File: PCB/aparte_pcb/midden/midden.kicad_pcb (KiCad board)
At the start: 2 copper layers, 211 x 207.2 mm, 39 parts, among them J1 Conn_01x10_Socket, J4 Conn_01x10_Socket, J5 Conn_01x04_Socket, K1 G5Q-1A, SW1 SW_Reed_SPDT, SW2 SW_DIP_x01

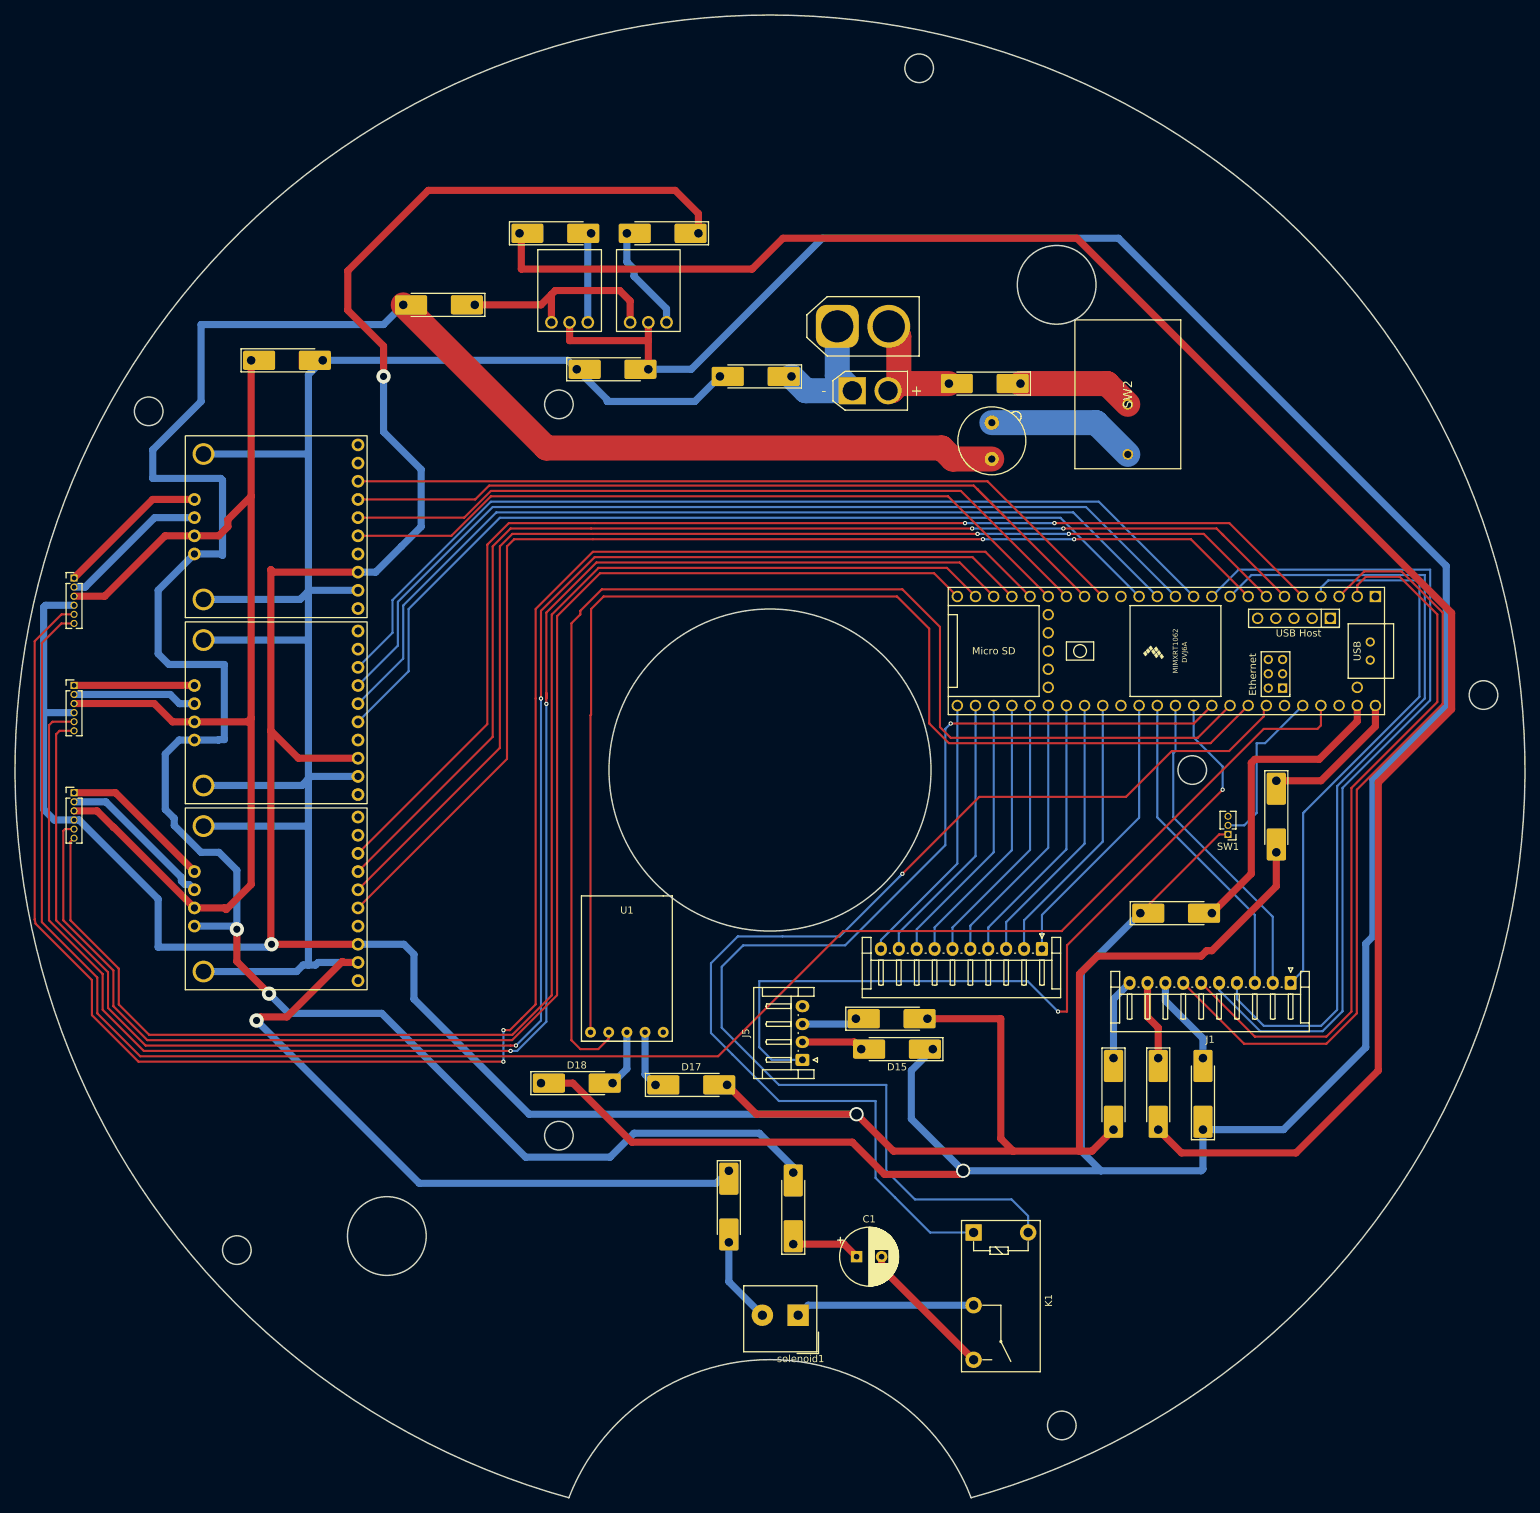
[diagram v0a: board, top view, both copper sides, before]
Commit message: schroef geaard
moet nog onderste schroef
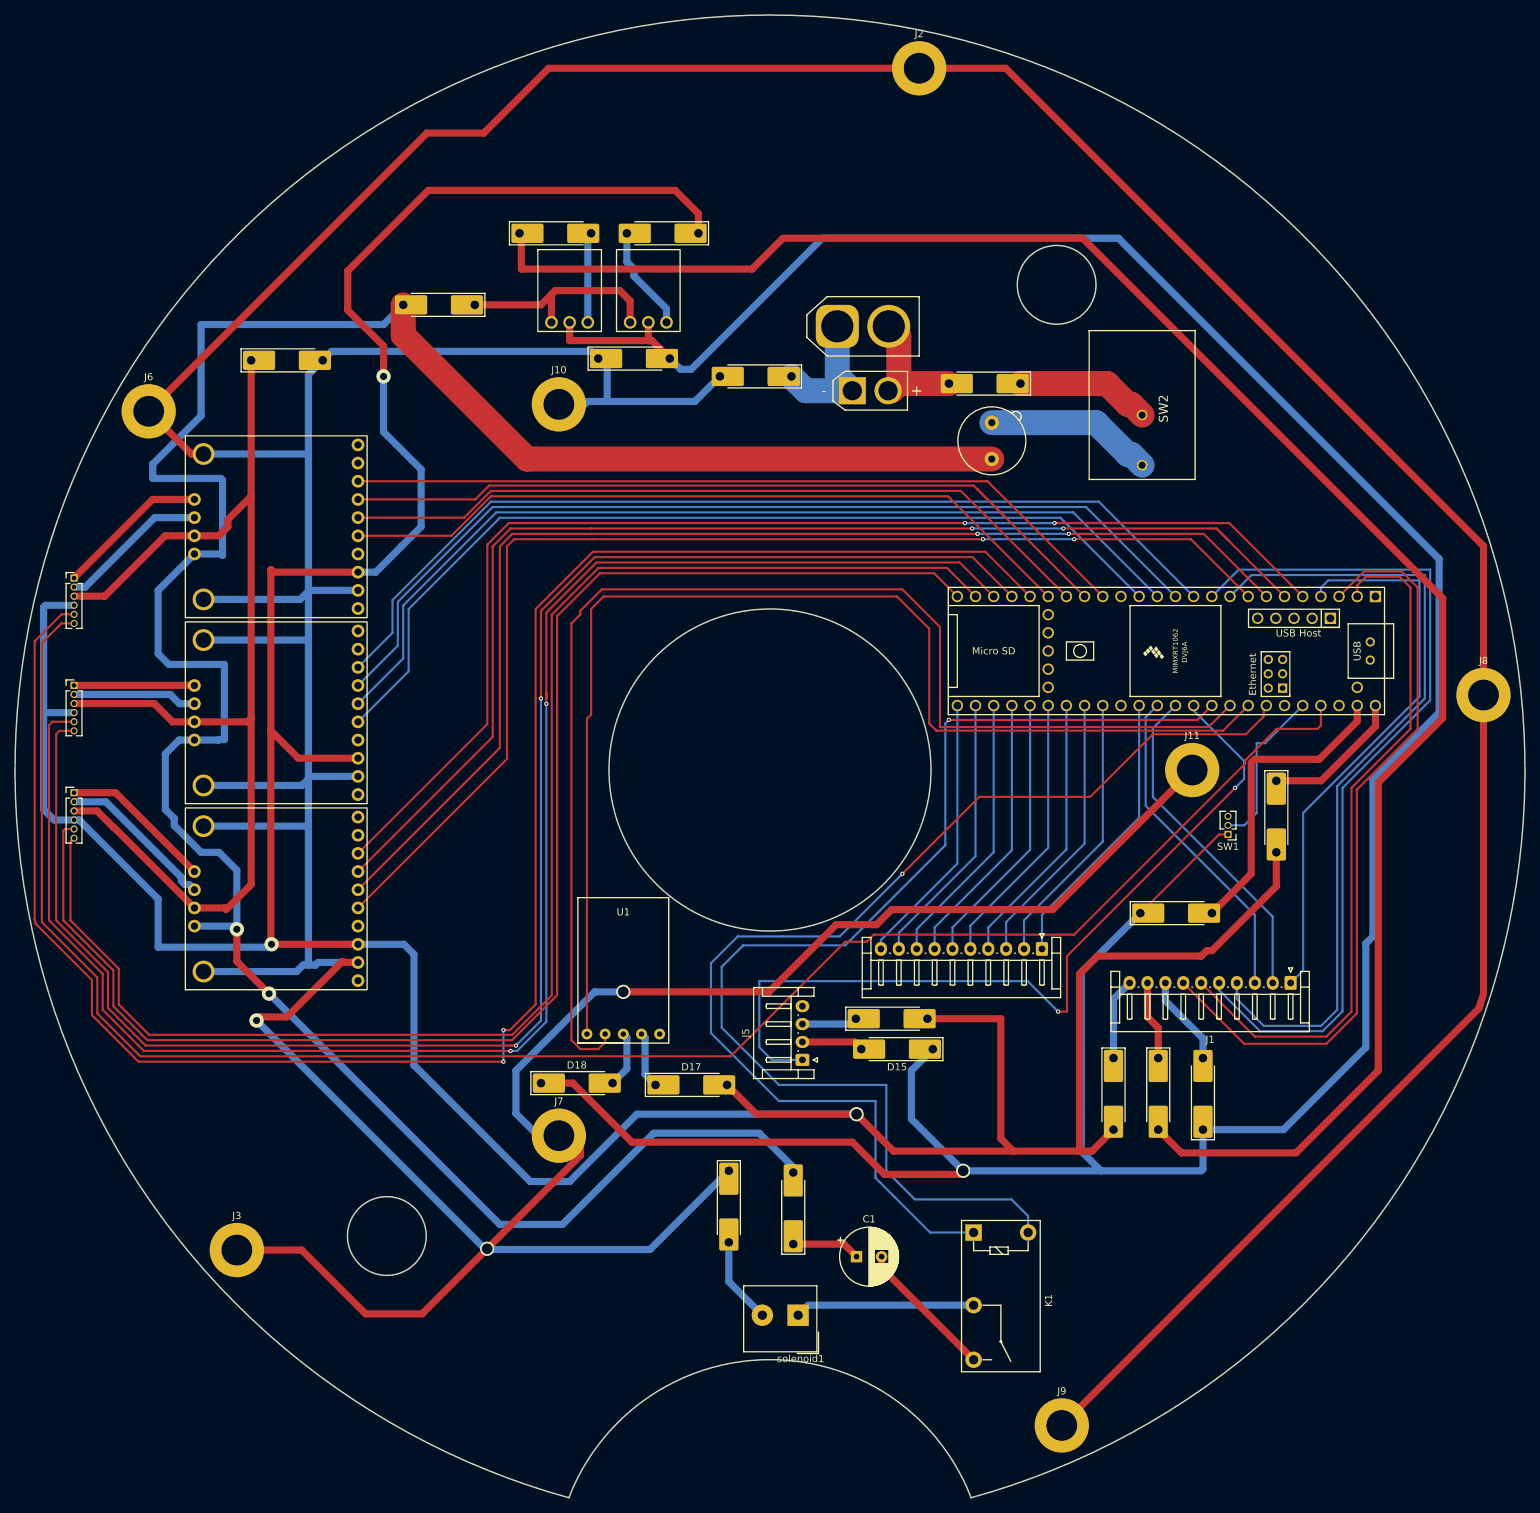
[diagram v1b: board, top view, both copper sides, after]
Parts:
- added J10: Screw_Terminal_01x01, MountingHole:MountingHole_4.3mm_M4_ISO7380_Pad, F.Cu at (120.5, 98.9)
- added J11: Screw_Terminal_01x01, MountingHole:MountingHole_4.3mm_M4_ISO7380_Pad, F.Cu at (209.0, 150.0)
- added J2: Screw_Terminal_01x01, MountingHole:MountingHole_4.3mm_M4_ISO7380_Pad, F.Cu at (170.8, 51.9)
- added J3: Screw_Terminal_01x01, MountingHole:MountingHole_4.3mm_M4_ISO7380_Pad, F.Cu at (75.5, 217.1)
- added J6: Screw_Terminal_01x01, MountingHole:MountingHole_4.3mm_M4_ISO7380_Pad, F.Cu at (63.2, 99.9)
- added J7: Screw_Terminal_01x01, MountingHole:MountingHole_4.3mm_M4_ISO7380_Pad, F.Cu at (120.5, 201.1)
- added J8: Screw_Terminal_01x01, MountingHole:MountingHole_4.3mm_M4_ISO7380_Pad, F.Cu at (249.7, 139.5)
- added J9: Screw_Terminal_01x01, MountingHole:MountingHole_4.3mm_M4_ISO7380_Pad, F.Cu at (190.8, 241.6)
- moved D7 3.35 mm to (131.0, 92.5)
- moved SW2 2.50 mm to (202.0, 100.4)
- moved U1 0.56 mm to (129.5, 184.3)
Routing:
- net Net-(D2-A): track 349.4 -> 945.7 mm, vias 1 -> 3
- net Net-(D12-A): track 514.4 -> 527.6 mm
- net Net-(D4-A): track 348.6 -> 358.9 mm
- net groundd: track 439.8 -> 436.6 mm
- net rx1: track 101.4 -> 98.3 mm
- net tx1: track 108.8 -> 105.9 mm
- net Net-(F1-Pad2): track 20.8 -> 23.5 mm
- net Net-(D1-K): track 16.2 -> 18.8 mm
- net BLAUW: track 114.2 -> 116.7 mm
- net Net-(DR3-PWM2): track 169.1 -> 171.5 mm
- net rx3: track 44.6 -> 47.0 mm
- net Net-(U1-sda): track 178.4 -> 176.7 mm
- net tx3: track 44.4 -> 45.7 mm
- net Net-(U1-scl): track 170.1 -> 169.1 mm
- net Net-(D11-A): track 263.6 -> 263.1 mm
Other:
- outline, holes or cut-outs redrawn

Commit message: dgsrf
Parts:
- added SW5: SW_Reed_SPDT, Library:Mini Snap-Action Switch with 13.5mm Lever 3-Pin, SPDT, 1A, F.Cu at (196.7, 217.5)
- 3V3_conv1, 5V_conv1: footprint Library:pololu-U1V10F5 -> Library:pololu-d30v30fx
- SW1: footprint Connector_PinHeader_1.27mm:PinHeader_1x03_P1.27mm_Vertical -> Library:Mini Snap-Action Switch with 13.5mm Lever 3-Pin, SPDT, 1A
- SW2: footprint dpdsd:R1966ABLKBLKEF -> Library:Rocker Switch 3-Pin, SPDT, 10A
- moved SW1 106.2 mm to (129.2, 223.0)
- moved D8 14.7 mm to (133.6, 60.4)
- moved 5V_conv1 9.46 mm to (141.3, 78.5)
- moved D9 9.18 mm to (122.5, 66.2)
- moved 3V3_conv1 4.64 mm to (123.3, 78.5)
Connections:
- teensy1 pad 43: unconnected-(teensy1-21_A7_RX5_BCLK1-Pad43) -> Net-(teensy1-21_A7_RX5_BCLK1)
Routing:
- net Net-(teensy1-22_A8_CTX1): track 23.1 -> 157.4 mm, vias 0 -> 6
- net Net-(teensy1-21_A7_RX5_BCLK1): track 0.00 -> 99.1 mm, vias 0 -> 4
- net groundd: track 436.6 -> 517.9 mm
- net Net-(D2-A): track 945.7 -> 968.3 mm
- net Net-(5V_conv1-VOUT): track 14.7 -> 35.5 mm
- net Net-(3V3_conv1-VIN): track 30.0 -> 46.4 mm
- net Net-(D1-A): track 17.5 -> 29.2 mm
- net Net-(3V3_conv1-VOUT): track 12.6 -> 24.1 mm
- net Net-(D2-K): track 19.2 -> 28.8 mm
- net Net-(D11-A): track 263.1 -> 267.4 mm
- net Net-(D4-A): track 358.9 -> 354.9 mm
- net Net-(F1-Pad2): track 23.5 -> 26.0 mm
- net Net-(D1-K): track 18.8 -> 21.3 mm
- net Net-(D12-A): track 527.6 -> 528.9 mm
